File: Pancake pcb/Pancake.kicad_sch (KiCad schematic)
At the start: 1 part, among them U1 RP2040

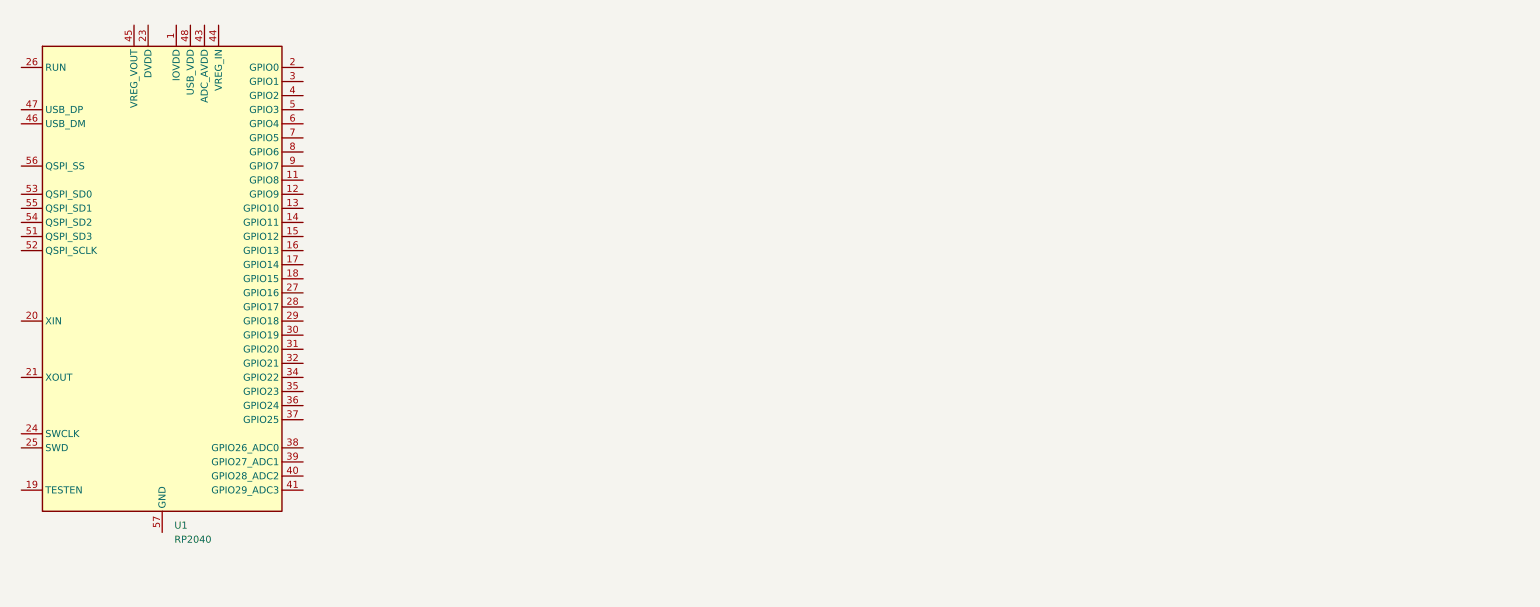
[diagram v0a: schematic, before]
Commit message: KLE and Datasheet
Add to the folder the datasheet of the RP2040 Pro Micro controller and the Keyboard Layout Editor files
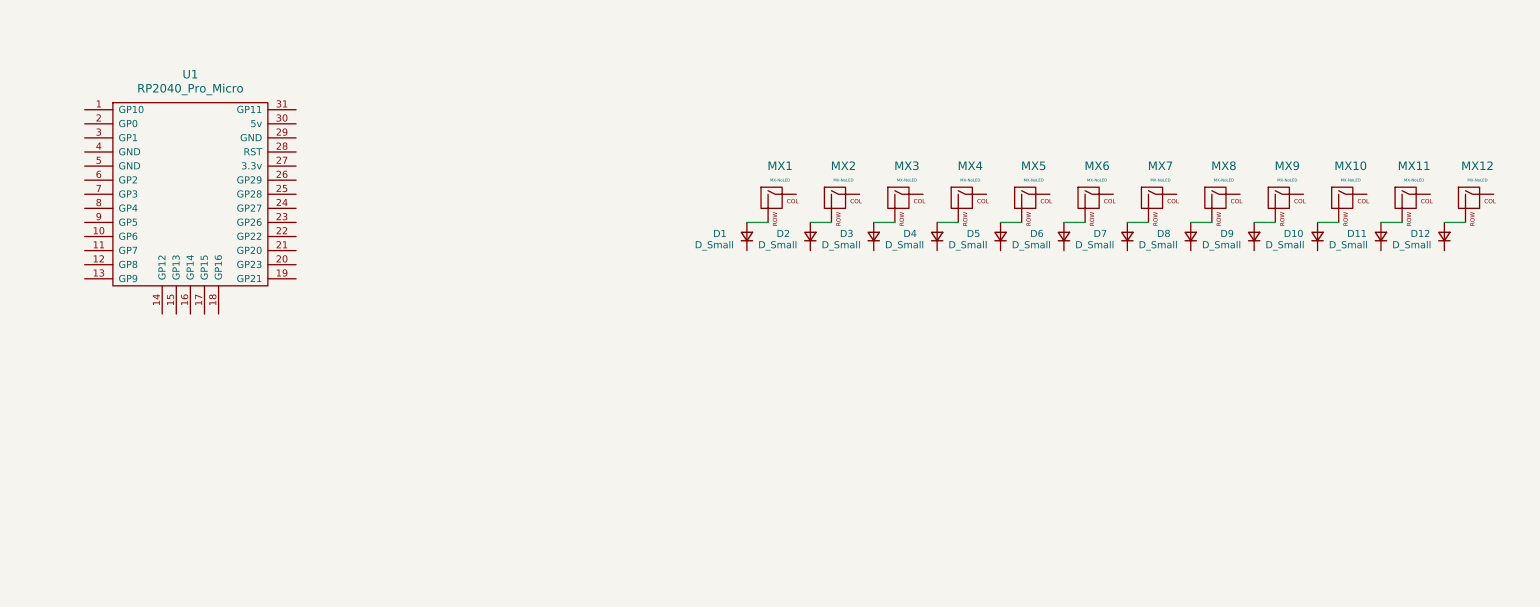
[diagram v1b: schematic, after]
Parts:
- removed U1: RP2040, Package_DFN_QFN:QFN-56-1EP_7x7mm_P0.4mm_EP3.2x3.2mm, symbol MCU_RaspberryPi:RP2040
- added D1, D10, D11, D12, D2, D3, D4, D5, D6, D7, D8, D9: D_Small, symbol Device:D_Small
- added MX1, MX10, MX11, MX12, MX2, MX3, MX4, MX5, MX6, MX7, MX8, MX9: MX-NoLED, symbol MX_Alps_Hybrid:MX-NoLED
- added U1: RP2040_Pro_Micro, ScottoKeebs_MCU:RP2040_Pro_Micro, symbol ScottoKeebs:MCU_RP2040_Pro_Micro
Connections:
- new net: D8.2 (A), MX8.2 (ROW)
- new net: D10.2 (A), MX10.2 (ROW)
- new net: D2.2 (A), MX2.2 (ROW)
- new net: D7.2 (A), MX7.2 (ROW)
- new net: D1.2 (A), MX1.2 (ROW)
- new net: D5.2 (A), MX5.2 (ROW)
- new net: D6.2 (A), MX6.2 (ROW)
- new net: D4.2 (A), MX4.2 (ROW)
- new net: D9.2 (A), MX9.2 (ROW)
- new net: D3.2 (A), MX3.2 (ROW)
- new net: D11.2 (A), MX11.2 (ROW)
- new net: D12.2 (A), MX12.2 (ROW)

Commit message: Lib modification
I change my library for my micro controller to use the RP2040 Pro Micro from 42Keebs
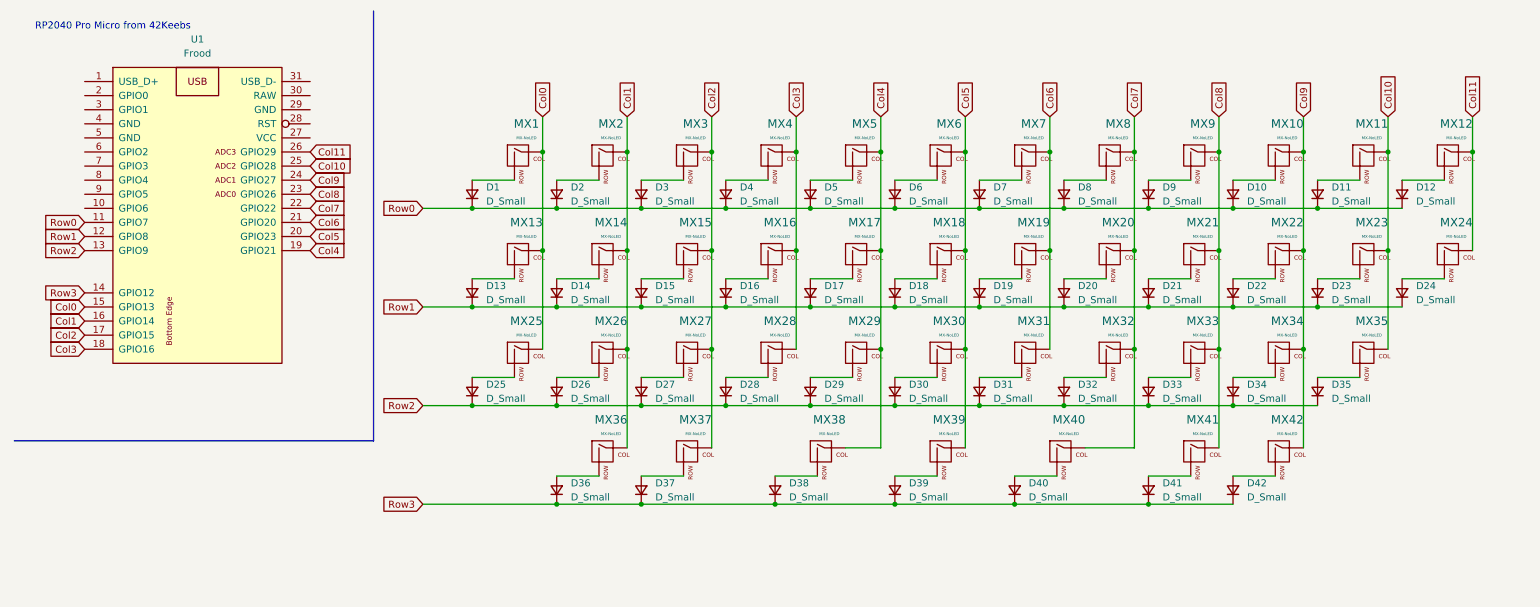
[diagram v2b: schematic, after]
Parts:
- removed U1: RP2040_Pro_Micro, ScottoKeebs_MCU:RP2040_Pro_Micro, symbol ScottoKeebs:MCU_RP2040_Pro_Micro
- added D13, D14, D15, D16, D17, D18, D19, D20, D21, D22, D23, D24, D25, D26, D27, D28, D29, D30, D31, D32, D33, D34, D35, D36, D37, D38, D39, D40, D41, D42: D_Small, symbol Device:D_Small
- added MX13, MX14, MX15, MX16, MX17, MX18, MX19, MX20, MX21, MX22, MX23, MX24, MX25, MX26, MX27, MX28, MX29, MX30, MX31, MX32, MX33, MX34, MX35, MX36, MX37, MX38, MX39, MX40, MX41, MX42: MX-NoLED, symbol MX_Alps_Hybrid:MX-NoLED
- added U1: Frood, 42keebs:Frood_PinHeader_2x13+5_P2.54mm_Labels_Top, symbol 42Keebs:Frood
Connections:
- net Row0: now reaches D8.1 (K)
- net Row0: now also D1.1 (K), D10.1 (K), D11.1 (K), D12.1 (K), D2.1 (K), D3.1 (K), D4.1 (K), D5.1 (K), D6.1 (K), D7.1 (K), D9.1 (K), U1.11 (GPIO7)
- net Col9: now reaches MX10.1 (COL)
- net Col9: now also MX22.1 (COL), MX34.1 (COL), MX42.1 (COL), U1.24 (GPIO27)
- net Col7: now reaches MX8.1 (COL)
- net Col7: now also MX20.1 (COL), MX32.1 (COL), MX40.1 (COL), U1.22 (GPIO22)
- net Col3: now reaches MX4.1 (COL)
- net Col3: now also MX16.1 (COL), MX28.1 (COL), U1.18 (GPIO16)
- net Col4: now reaches MX5.1 (COL)
- net Col4: now also MX17.1 (COL), MX29.1 (COL), MX38.1 (COL), U1.19 (GPIO21)
- net Col0: now reaches MX1.1 (COL)
- net Col0: now also MX13.1 (COL), MX25.1 (COL), U1.15 (GPIO13)
- net Col6: now reaches MX7.1 (COL)
- net Col6: now also MX19.1 (COL), MX31.1 (COL), U1.21 (GPIO20)
- net Col2: now reaches MX3.1 (COL)
- net Col2: now also MX15.1 (COL), MX27.1 (COL), MX37.1 (COL), U1.17 (GPIO15)
- net Col10: now reaches MX11.1 (COL)
- net Col10: now also MX23.1 (COL), MX35.1 (COL), U1.25 (GPIO28)
- net Col11: now reaches MX12.1 (COL)
- net Col11: now also MX24.1 (COL), U1.26 (GPIO29)
- net Col1: now reaches MX2.1 (COL)
- net Col1: now also MX14.1 (COL), MX26.1 (COL), MX36.1 (COL), U1.16 (GPIO14)
- net Col5: now reaches MX6.1 (COL)
- net Col5: now also MX18.1 (COL), MX30.1 (COL), MX39.1 (COL), U1.20 (GPIO23)
- net Col8: now reaches MX9.1 (COL)
- net Col8: now also MX21.1 (COL), MX33.1 (COL), MX41.1 (COL), U1.23 (GPIO26)
- new net: D41.2 (A), MX41.2 (ROW)
- new net: D24.2 (A), MX24.2 (ROW)
- new net: D25.2 (A), MX25.2 (ROW)
- new net: D29.2 (A), MX29.2 (ROW)
- new net: D14.2 (A), MX14.2 (ROW)
- new net: D17.2 (A), MX17.2 (ROW)
- new net: D23.2 (A), MX23.2 (ROW)
- new net: D26.2 (A), MX26.2 (ROW)
- new net: D30.2 (A), MX30.2 (ROW)
- new net: D42.2 (A), MX42.2 (ROW)
- new net: D28.2 (A), MX28.2 (ROW)
- new net: D37.2 (A), MX37.2 (ROW)
- new net: D31.2 (A), MX31.2 (ROW)
- new net: D20.2 (A), MX20.2 (ROW)
- new net: D33.2 (A), MX33.2 (ROW)
- new net: D18.2 (A), MX18.2 (ROW)
- new net: D15.2 (A), MX15.2 (ROW)
- new net: D36.2 (A), MX36.2 (ROW)
- new net: D38.2 (A), MX38.2 (ROW)
- new net: D40.2 (A), MX40.2 (ROW)
- new net: D16.2 (A), MX16.2 (ROW)
- new net: D22.2 (A), MX22.2 (ROW)
- new net: D35.2 (A), MX35.2 (ROW)
- new net: D19.2 (A), MX19.2 (ROW)
- new net: D21.2 (A), MX21.2 (ROW)
- new net: D34.2 (A), MX34.2 (ROW)
- new net: D27.2 (A), MX27.2 (ROW)
- new net: D13.2 (A), MX13.2 (ROW)
- new net: D39.2 (A), MX39.2 (ROW)
- new net: D32.2 (A), MX32.2 (ROW)
- new net Row1: D13.1 (K), D14.1 (K), D15.1 (K), D16.1 (K), D17.1 (K), D18.1 (K), D19.1 (K), D20.1 (K), D21.1 (K), D22.1 (K), D23.1 (K), D24.1 (K), U1.12 (GPIO8)
- new net Row2: D25.1 (K), D26.1 (K), D27.1 (K), D28.1 (K), D29.1 (K), D30.1 (K), D31.1 (K), D32.1 (K), D33.1 (K), D34.1 (K), D35.1 (K), U1.13 (GPIO9)
- new net Row3: D36.1 (K), D37.1 (K), D38.1 (K), D39.1 (K), D40.1 (K), D41.1 (K), D42.1 (K), U1.14 (GPIO12)
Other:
- note added: "RP2040 Pro Micro from 42Keebs"
- moved on the sheet: MX1

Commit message: A lot of modification
addition of a jst cable and other
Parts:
- added J1: Conn_01x04, Connector_JST:JST_SH_BM04B-SRSS-TB_1x04-1MP_P1.00mm_Vertical, symbol PCM_4ms_Connector:Conn_01x04
- D1, D10, D11, D12, D13, D14, D15, D16, D17, D18, D19, D2, D20, D21, D22, D23, D24, D25, D26, D27, D28, D29, D3, D30, D31, D32, D33, D34, D35, D36, D37, D38, D39, D4, D40, D41, D42, D5, D6, D7, D8, D9: footprint (none) -> Diode_SMD:D_SOD-123
- MX1, MX10, MX11, MX14, MX15, MX16, MX17, MX18, MX19, MX2, MX20, MX21, MX22, MX23, MX24, MX26, MX27, MX28, MX29, MX3, MX30, MX31, MX32, MX33, MX34, MX37, MX39, MX4, MX41, MX5, MX6, MX7, MX8, MX9: footprint (none) -> ScottoKeebs_MX:MX_PCB_1.00u
- MX12, MX13, MX35, MX36, MX42: footprint (none) -> ScottoKeebs_MX:MX_PCB_1.25u
- MX25: footprint (none) -> ScottoKeebs_MX:MX_PCB_1.50u
- MX38, MX40: footprint (none) -> ScottoKeebs_MX:MX_PCB_2.00u
- U1: footprint 42keebs:Frood_PinHeader_2x13+5_P2.54mm_Labels_Top -> footprints:Frood_PinHeader_2x13+5_P2.54mm_Labels_Top
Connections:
- net Col0: now also U1.19 (GPIO21); no longer U1.15 (GPIO13)
- net Col1: now also U1.18 (GPIO16); no longer U1.16 (GPIO14)
- net Col10: now also U1.8 (GPIO4); no longer U1.25 (GPIO28)
- net Col11: now also U1.7 (GPIO3); no longer U1.26 (GPIO29)
- net Col3: now also U1.16 (GPIO14); no longer U1.18 (GPIO16)
- net Col4: now also U1.15 (GPIO13); no longer U1.19 (GPIO21)
- net Col5: now also U1.14 (GPIO12); no longer U1.20 (GPIO23)
- net Col6: now also U1.13 (GPIO9); no longer U1.21 (GPIO20)
- net Col7: now also U1.12 (GPIO8); no longer U1.22 (GPIO22)
- net Col8: now also U1.11 (GPIO7); no longer U1.23 (GPIO26)
- net Col9: now also U1.9 (GPIO5); no longer U1.24 (GPIO27)
- net Row0: now also U1.2 (GPIO0); no longer U1.11 (GPIO7)
- net Row1: now also U1.3 (GPIO1); no longer U1.12 (GPIO8)
- net Row2: now also U1.6 (GPIO2); no longer U1.13 (GPIO9)
- net Row3: now also U1.10 (GPIO6); no longer U1.14 (GPIO12)
- net D+: now reaches U1.1 (USB_D+)
- net D+: now also J1.3 (Pin_3)
- net GND: now reaches U1.29 (GND)
- net GND: now also U1.4 (GND), U1.5 (GND), J1.4 (Pin_4)
- net RAW: now reaches U1.30 (RAW)
- net RAW: now also J1.1 (Pin_1)
- net D-: now reaches U1.31 (USB_D-)
- net D-: now also J1.2 (Pin_2)
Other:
- note added: "JST connector"
- note added: "Keymap"
- moved on the sheet: D1, D10, D11, D12, D13, D14, D15, D16, D17, D18, D19, D2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
